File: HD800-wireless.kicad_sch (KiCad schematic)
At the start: 0 parts

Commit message: commit before dk firmware test
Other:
- added sheet 01 USB Charging (01_USB_Charging.kicad_sch)
- added sheet 02 Power (02_Power.kicad_sch)
- added sheet 03 MCU RF (03_MCU_RF.kicad_sch)
- added sheet 04 DAC L (04_DAC_Left.kicad_sch)
- added sheet 05 DAC R (04_DAC_Left.kicad_sch)
- added sheet 06 Balanced Output (06_Balanced_Output.kicad_sch)
- note added: "250mW output, 130dBA system performance, <10ms latency and 33/47h runtime are targets, not measurements."
- note added: "Battery -> 1.8V buck / DAC VP Turbo only: Q1 -> positive rail + LM2776 negative rail"
- note added: "DESIGN STATUS / REQUIRED BEFORE PCB RELEASE"
- note added: "Dual CS43131 / nRF5340 / assembly-configured Eco or Turbo"
- note added: "ECO assembly: DACs -> configuration links -> drivers TURBO assembly: DACs -> 4 buffers -> links -> drivers"
- note added: "Functional draft: six connected circuit sheets, custom symbols, netlist validation and review notes."
- note added: "HD800 WIRELESS"
- note added: "No headphone jack or BGA audio muxes: four solder pads wire directly to the installed drivers."
- note added: "RF matching, battery thermal/current limits, USB-C charge policy and amplifier load stability need validation."
- note added: "SIGNAL FLOW"
- note added: "See DESIGN_NOTES.md for Eco/Turbo population links, sources and remaining release blockers."
- note added: "USB / 2.4GHz -> nRF5340 -> I2S + I2C -> two CS43131 DACs -> 4 balanced audio legs"
- title: (none) -> HD800 WIRELESS | system overview

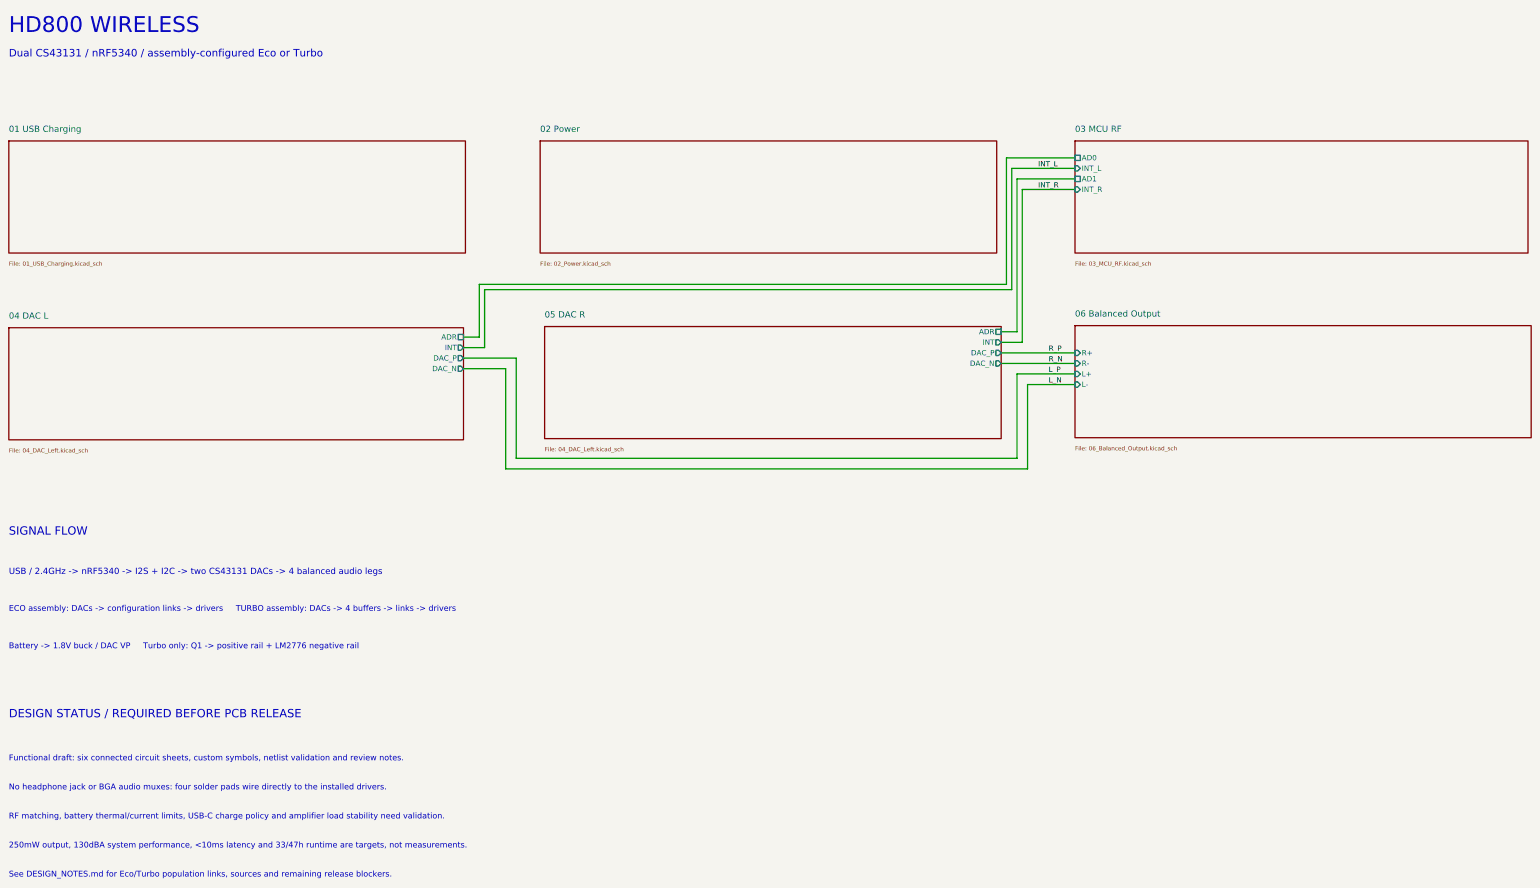
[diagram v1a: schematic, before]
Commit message: removed firmware
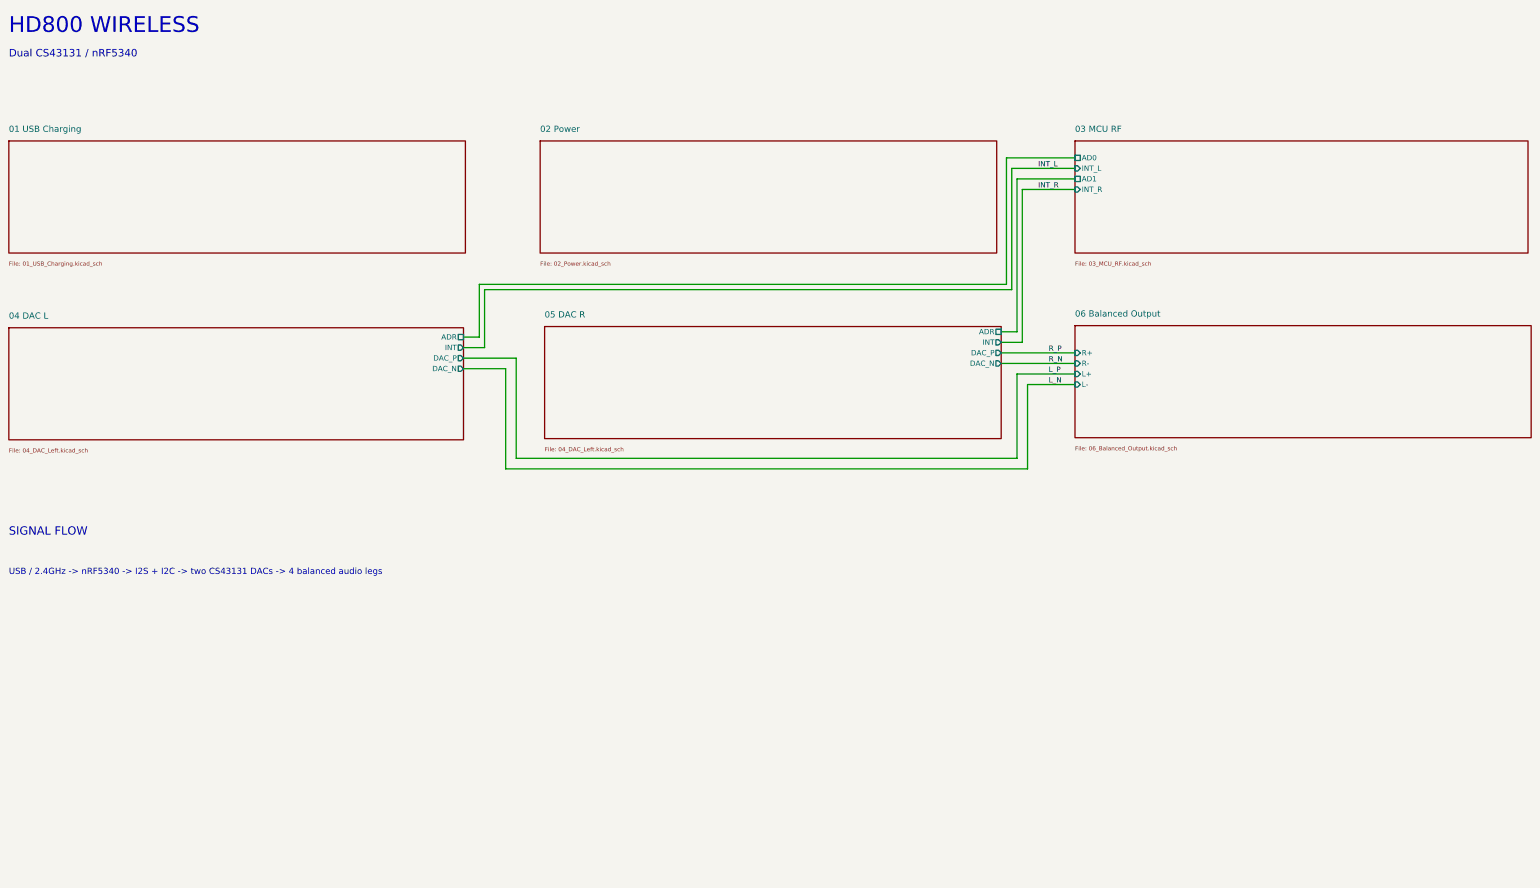
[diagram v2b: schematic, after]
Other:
- note added: "Dual CS43131 / nRF5340"
- note removed: "250mW output, 130dBA system performance, <10ms latency and 33/47h runtime are targets, not measurements."
- note removed: "Battery -> 1.8V buck / DAC VP Turbo only: Q1 -> positive rail + LM2776 negative rail"
- note removed: "DESIGN STATUS / REQUIRED BEFORE PCB RELEASE"
- note removed: "Dual CS43131 / nRF5340 / assembly-configured Eco or Turbo"
- note removed: "ECO assembly: DACs -> configuration links -> drivers TURBO assembly: DACs -> 4 buffers -> links -> drivers"
- note removed: "Functional draft: six connected circuit sheets, custom symbols, netlist validation and review notes."
- note removed: "No headphone jack or BGA audio muxes: four solder pads wire directly to the installed drivers."
- note removed: "RF matching, battery thermal/current limits, USB-C charge policy and amplifier load stability need validation."
- note removed: "See DESIGN_NOTES.md for Eco/Turbo population links, sources and remaining release blockers."
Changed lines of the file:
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@@
 		(comment 1 "NOT FOR FABRICATION - see DESIGN_NOTES.md")
-	)
-	(text "No headphone jack or BGA audio muxes: four solder pads wire directly to the installed drivers."
-		(exclude_from_sim no)
-		(at 20 203 0)
-		(effects
-			(font
-				(size 1.4 1.4)
-			)
-			(justify left top)
-		)
-	)
-	(text "Functional draft: six connected circuit sheets, custom symbols, netlist validation and review notes."
-		(exclude_from_sim no)
-		(at 20 196 0)
-		(effects
-			(font
-				(size 1.4 1.4)
-			)
-			(justify left top)
-		)
 	)
 	(text "USB / 2.4GHz -> nRF5340 -> I2S + I2C -> two CS43131 DACs -> 4 balanced audio legs"
@@
 		)
 	)
-	(text "Battery -> 1.8V buck / DAC VP     Turbo only: Q1 -> positive rail + LM2776 negative rail"
-		(exclude_from_sim no)
-		(at 20 169 0)
-		(effects
-			(font
-				(size 1.4 1.4)
-			)
-			(justify left top)
-		)
-	)
-	(text "Dual CS43131 / nRF5340 / assembly-configured Eco or Turbo"
+	(text "Dual CS43131 / nRF5340"
 		(exclude_from_sim no)
 		(at 20 26 0)
@@
 			(font
 				(size 1.8 1.8)
-			)
-			(justify left top)
-		)
-	)
-	(text "DESIGN STATUS / REQUIRED BEFORE PCB RELEASE"
-		(exclude_from_sim no)
-		(at 20 185 0)
-		(effects
-			(font
-				(size 2 2)
 			)
 			(justify left top)
@@
 			)
 			(justify left top)
-		)
-	)
-	(text "ECO assembly: DACs -> configuration links -> drivers     TURBO assembly: DACs -> 4 buffers -> links -> drivers"
-		(exclude_from_sim no)
-		(at 20 160 0)
-		(effects
-			(font
-				(size 1.4 1.4)
-			)
-			(justify left top)
-		)
-	)
-	(text "250mW output, 130dBA system performance, <10ms latency and 33/47h runtime are targets, not measurements."
-		(exclude_from_sim no)
-		(at 20 217 0)
-		(effects
-			(font
-				(size 1.4 1.4)
-			)
-			(justify left top)
-		)
-	)
-	(text "RF matching, battery thermal/current limits, USB-C charge policy and amplifier load stability need validation."
-		(exclude_from_sim no)
-		(at 20 210 0)
-		(effects
-			(font
-				(size 1.4 1.4)
-			)
-			(justify left top)
-		)
-	)
-	(text "See DESIGN_NOTES.md for Eco/Turbo population links, sources and remaining release blockers."
-		(exclude_from_sim no)
-		(at 20 224 0)
-		(effects
-			(font
-				(size 1.4 1.4)
-			)
-			(justify left top)
